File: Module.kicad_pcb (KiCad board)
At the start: 6 copper layers, 30 x 41.8 mm, 128 parts, among them J2 HOLDDOWN, Q1 FDN86246, Q2 VOS617A-7T, T1 POE70P-50L, T2 S558-5500-25-F, U1 TPS23753APW, U2 74AUP1G07, U3 TLV431ACDBZR, U4 LAN8720A, U5 ESP32-D0WD, U6 W25Q128JVP, U7 APS6404L-3SQR-ZR, U8 TPS259520DSGR, Y1 ECS-2333-500-BN-TR, Y2 40.000 MHz

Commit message: all parts geo-renamed
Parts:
- renumbered C18 to 1C1, C49 to 1C10, C39 to 1C11, C38 to 1C12, C37 to 1C13, C23 to 1C14, C6 to 1C2, C24 to 1C3, C5 to 1C4, C25 to 1C5, C2 to 1C6, C10 to 1C7, C1 to 1C8, C34 to 1C9, D4 to 1D1, D8 to 1D2, D1 to 1D3, J2 to 1J1, J1 to 1J2, L1 to 1L1, L2 to 1L2, R7 to 1R1, R28 to 1R2, R45 to 1R3, R31 to 1R4, R27 to 1R5, R39 to 1R6, R46 to 1R7, R41 to 1R8, T1 to 1T1, T2 to 1T2, TP1 to 1TP1, U4 to 1U1, U6 to 1U2, U2 to 1U3, U5 to 1U4, U8 to 1U5, C15 to 2C1, C33 to 2C10, C17 to 2C11, C31 to 2C12, C35 to 2C13, C32 to 2C14, C50 to 2C15, C22 to 2C16, C8 to 2C17, C16 to 2C18, C53 to 2C19, C14 to 2C2, C52 to 2C20, C54 to 2C21, C51 to 2C22, C47 to 2C23, C27 to 2C24, C30 to 2C25, C20 to 2C26, C26 to 2C27, C44 to 2C28, C48 to 2C29, C4 to 2C3, C42 to 2C30, C19 to 2C31, C46 to 2C32, C41 to 2C33, C29 to 2C34, C21 to 2C35, C45 to 2C36, C43 to 2C37, C36 to 2C38, C28 to 2C39, C3 to 2C4, C11 to 2C5, C13 to 2C6, C7 to 2C7, C12 to 2C8, C9 to 2C9, D3 to 2D1, D5 to 2D2, D9 to 2D3, D10 to 2D4, D6 to 2D5, D2 to 2D6, Q2 to 2Q1, Q1 to 2Q2, R18 to 2R1, R15 to 2R10, R17 to 2R11, R11 to 2R12, R32 to 2R13, R8 to 2R14, R30 to 2R15, R34 to 2R16, R33 to 2R17, R35 to 2R18, R29 to 2R19, R12 to 2R2, R42 to 2R20, R3 to 2R21, R5 to 2R22, R1 to 2R23, R6 to 2R24, R2 to 2R25, R36 to 2R26, R37 to 2R27, R38 to 2R28, R19 to 2R29, R44 to 2R3, R25 to 2R30, R24 to 2R31, R26 to 2R32, R23 to 2R33, R14 to 2R34, R22 to 2R35, R40 to 2R36, R20 to 2R37, R43 to 2R38, R9 to 2R4, R13 to 2R5, R10 to 2R6, R4 to 2R7, R16 to 2R8, R21 to 2R9, U3 to 2U1, U1 to 2U2, U7 to 2U3, Y1 to 2Y1, Y2 to 2Y2

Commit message: properties cleanup added unique parts ID
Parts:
- 2U3: value APS6404L-3SQR-ZR -> APS6404L-3SQR-SN

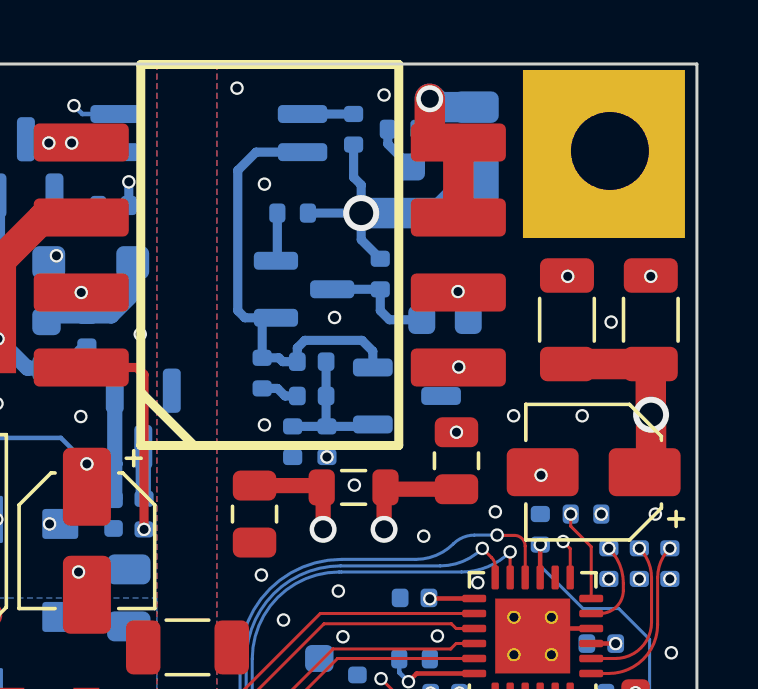
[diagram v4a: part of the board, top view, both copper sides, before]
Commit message: fixed wrong flyback transformer pinout
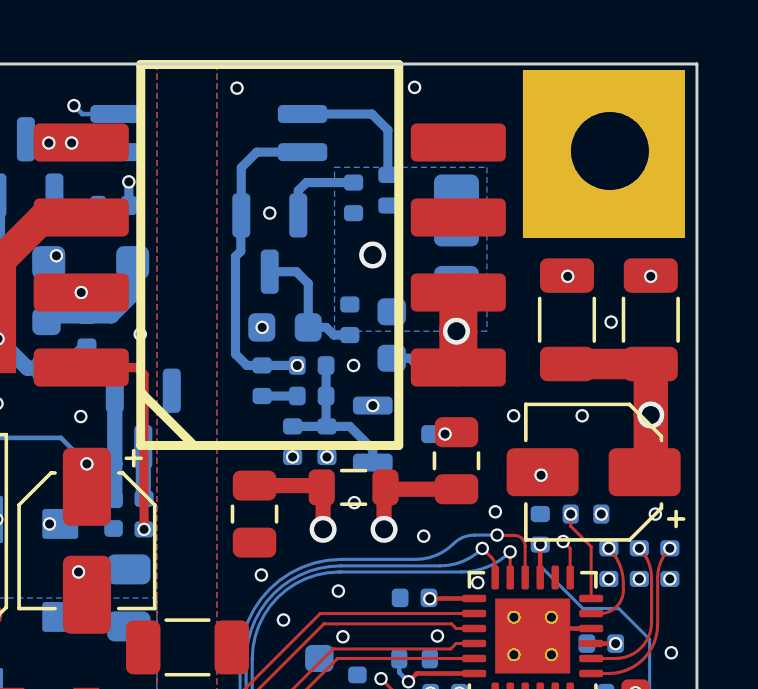
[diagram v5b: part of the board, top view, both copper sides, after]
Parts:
- moved 2R1 8.02 mm to (6.73, -31.8)
- moved 2C2 5.34 mm to (1.27, -33.0), turned to 0 degrees
- moved 2C1 4.87 mm to (4.83, -32.8), turned to 90 degrees
- moved 2D1 2.85 mm to (6.99, -36.1), turned to -90 degrees
- moved 2R2 2.33 mm to (4.70, -37.6)
- moved 2R3 2.09 mm to (3.56, -37.3), turned to 90 degrees
- moved 2D3 1.91 mm to (0.76, -35.8), turned to -90 degrees
- moved 2R5 1.83 mm to (3.43, -33.3)
- moved 2U1 1.27 mm to (5.33, -29.5)
- moved 2R8 0.25 mm to (0.51, -31.2)
- moved 2C5 0.13 mm to (2.16, -31.8)
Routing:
- net /Vout: track 58.2 -> 47.8 mm
- net Net-(2Q1-Pad1): track 1.70 -> 4.56 mm
- net Net-(2D1-A): track 7.47 -> 5.40 mm
- net Net-(2U1-K): track 15.2 -> 13.8 mm, vias 0 -> 2
- net Net-(2D3-A): track 1.61 -> 2.78 mm
- net Net-(2U1-FB): track 4.87 -> 5.47 mm
- net Net-(2C2-Pad2): track 3.82 -> 4.40 mm
- net GND: vias 59 -> 58
- added copper zone on B.Cu, net /Vout

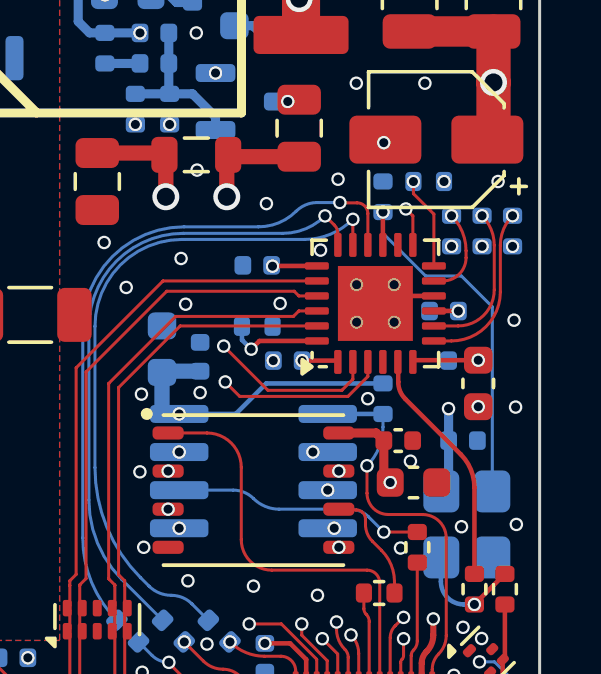
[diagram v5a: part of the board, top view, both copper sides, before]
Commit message: moved bottom 0402 resistors away from board edge
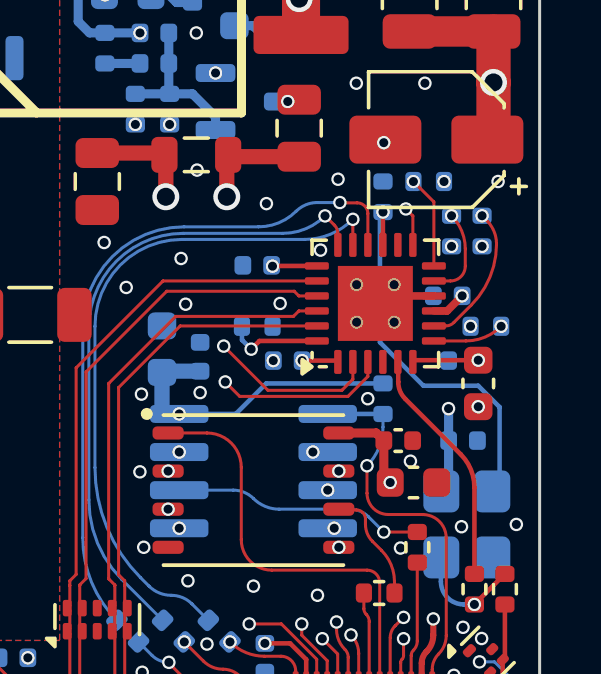
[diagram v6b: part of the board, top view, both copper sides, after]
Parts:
- moved 2R16 3.30 mm to (13.2, -22.0), turned to 0 degrees
- moved 2C12 0.52 mm to (11.9, -23.0)
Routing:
- net /Ethernet/RXD1: track 25.4 -> 22.0 mm
- net Net-(1U1-RXD1/MODE1): track 5.72 -> 2.37 mm
- net /PHY_EN: track 49.0 -> 49.6 mm
- net GND: vias 58 -> 56
